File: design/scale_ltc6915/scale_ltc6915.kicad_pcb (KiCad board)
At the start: 2 copper layers, 70 x 40 mm, 76 parts, among them J1 USB_B_Micro, J2 Conn_02x03_Odd_Even, J3 Load cell, J4 Conn_01x04, Q1 IRLML6401, Q2 AO3400, Q3 AO3400, SW1 SW_SPST, SW2 ON/OFF switch, U1 MDBT42Q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

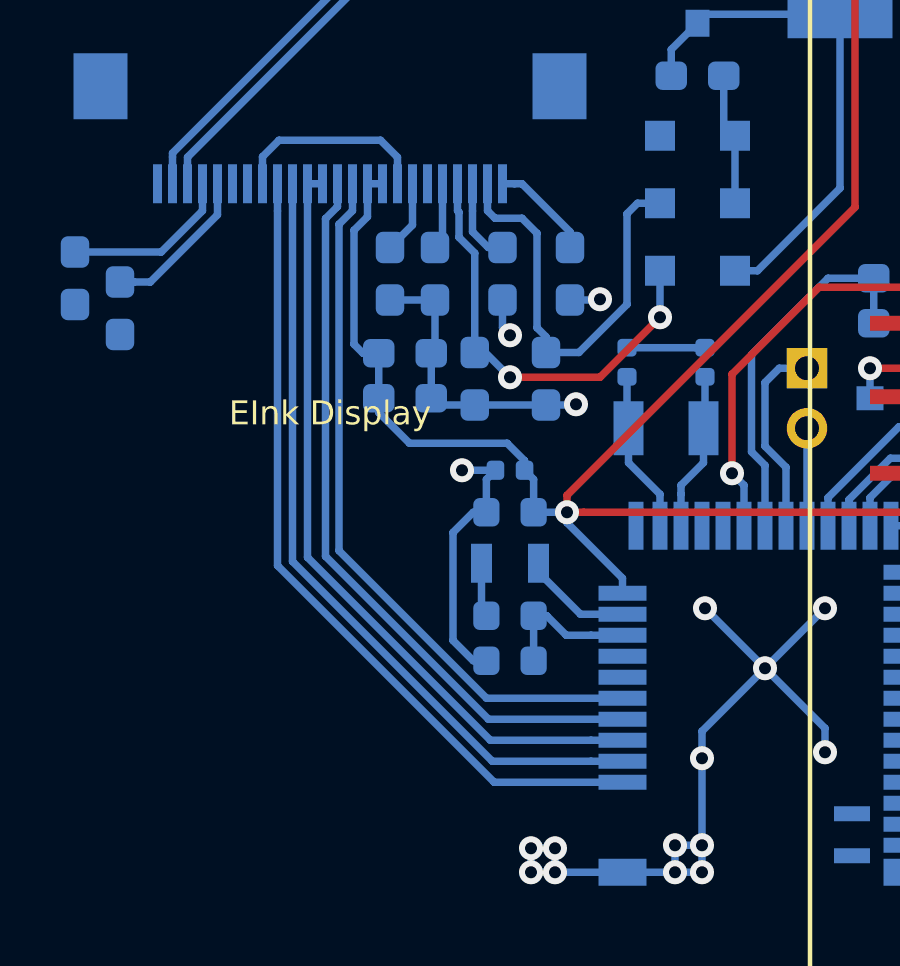
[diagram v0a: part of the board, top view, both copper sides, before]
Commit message: DC, CS pins separated, issue fixed. In both scale_hx711 and scale_ltc6915.
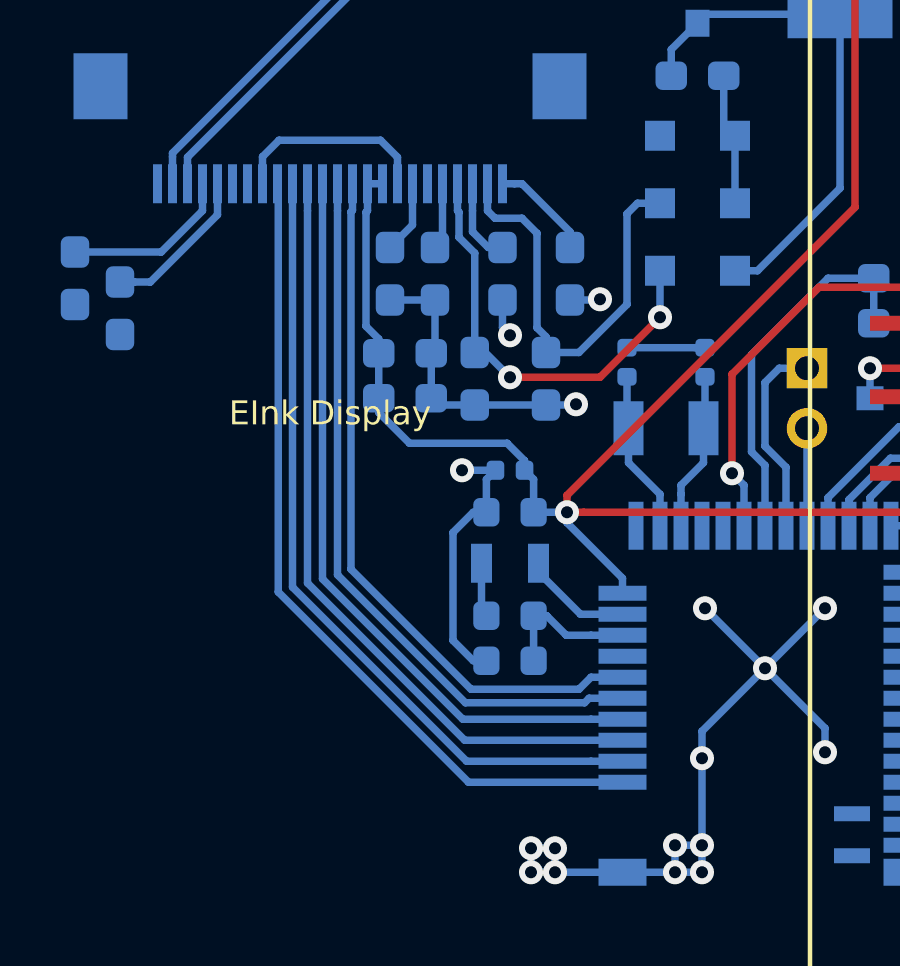
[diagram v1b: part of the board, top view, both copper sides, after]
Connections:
- EINK1 pad 11: /Sheet5E60241E/EINK_CS -> /Sheet5E60241E/EINK_DS
- U1 pad 4: /Sheet5E60241E/EINK_CS -> /Sheet5E60241E/EINK_DS
- U1 pad 5: /Sheet5E60241E/EINK_SCLK -> /Sheet5E60241E/EINK_CS
- U1 pad 6: /Sheet5E60241E/EINK_SDIO -> /Sheet5E60241E/EINK_SCLK
- U1 pad 7: (no net) -> /Sheet5E60241E/EINK_SDIO
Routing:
- net /Sheet5E60241E/EINK_DS: track 0.00 -> 26.0 mm
- net /Sheet5E60241E/EINK_CS: track 26.0 -> 25.1 mm
- net VDD: track 100.6 -> 100.0 mm
- net /Sheet5E60241E/EINK_RST: track 26.3 -> 26.8 mm
- net /Sheet5E60241E/EINK_BUSY: track 27.2 -> 27.7 mm
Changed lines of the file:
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@@
     (thickness 1.6)
     (drawings 17)
-    (tracks 583)
+    (tracks 589)
     (zones 0)
     (modules 76)
-    (nets 64)
+    (nets 65)
   )
   (page A4)
@@
   (net 62 /nRF/BT_LVL_EN)
   (net 63 /nRF/BAT_LVL)
+  (net 64 /Sheet5E60241E/EINK_DS)
   (net_class Default "This is the default net class."
     (clearance 0.2)
@@
     (add_net /Sheet5E60241E/EINK_BUSY)
     (add_net /Sheet5E60241E/EINK_CS)
+    (add_net /Sheet5E60241E/EINK_DS)
     (add_net /Sheet5E60241E/EINK_RST)
     (add_net /Sheet5E60241E/EINK_SCLK)
@@
       (net 40 /Sheet5E60241E/EINK_RST))
     (pad 11 smd rect (at -0.75 1.85) (size 0.3 1.3) (layers B.Cu B.Paste B.Mask)
-      (net 23 /Sheet5E60241E/EINK_CS))
+      (net 64 /Sheet5E60241E/EINK_DS))
     (pad 12 smd rect (at -0.25 1.85) (size 0.3 1.3) (layers B.Cu B.Paste B.Mask)
       (net 23 /Sheet5E60241E/EINK_CS))
@@
       (net 3 /nRF/DEC4))
     (pad 8 smd rect (at -4.75 -1.9) (size 1.6 0.5) (layers B.Cu B.Paste B.Mask))
-    (pad 7 smd rect (at -4.75 -1.2) (size 1.6 0.5) (layers B.Cu B.Paste B.Mask))
-    (pad 6 smd rect (at -4.75 -0.5) (size 1.6 0.5) (layers B.Cu B.Paste B.Mask)
+    (pad 7 smd rect (at -4.75 -1.2) (size 1.6 0.5) (layers B.Cu B.Paste B.Mask)
       (net 42 /Sheet5E60241E/EINK_SDIO))
-    (pad 5 smd rect (at -4.75 0.2) (size 1.6 0.5) (layers B.Cu B.Paste B.Mask)
+    (pad 6 smd rect (at -4.75 -0.5) (size 1.6 0.5) (layers B.Cu B.Paste B.Mask)
       (net 41 /Sheet5E60241E/EINK_SCLK))
-    (pad 4 smd rect (at -4.75 0.9) (size 1.6 0.5) (layers B.Cu B.Paste B.Mask)
+    (pad 5 smd rect (at -4.75 0.2) (size 1.6 0.5) (layers B.Cu B.Paste B.Mask)
       (net 23 /Sheet5E60241E/EINK_CS))
+    (pad 4 smd rect (at -4.75 0.9) (size 1.6 0.5) (layers B.Cu B.Paste B.Mask)
+      (net 64 /Sheet5E60241E/EINK_DS))
     (pad 3 smd rect (at -4.75 1.6) (size 1.6 0.5) (layers B.Cu B.Paste B.Mask)
       (net 40 /Sheet5E60241E/EINK_RST))
@@
   (segment (start 48.5 13.5) (end 49 13) (width 0.25) (layer B.Cu) (net 5))
   (segment (start 33.25 22.85) (end 32.75 22.85) (width 0.25) (layer B.Cu) (net 5))
-  (segment (start 32.75 22.85) (end 32.75 23.95) (width 0.25) (layer B.Cu) (net 5))
-  (segment (start 32.75 23.95) (end 32.3 24.4) (width 0.25) (layer B.Cu) (net 5))
-  (segment (start 32.6 28.5) (end 33.125 28.5) (width 0.25) (layer B.Cu) (net 5))
-  (segment (start 32.3 28.2) (end 32.6 28.5) (width 0.25) (layer B.Cu) (net 5))
-  (segment (start 32.3 24.4) (end 32.3 28.2) (width 0.25) (layer B.Cu) (net 5))
   (via (at 39.4 33.8) (size 0.8) (drill 0.4) (layers F.Cu B.Cu) (net 5))
   (segment (start 39.4 34.15) (end 39.4 33.8) (width 0.25) (layer B.Cu) (net 5))
@@
   (segment (start 66.2 11.6) (end 65.7 12.1) (width 0.25) (layer B.Cu) (net 5))
   (segment (start 67.6 11.6) (end 66.2 11.6) (width 0.25) (layer B.Cu) (net 5))
+  (segment (start 33.125 28.025) (end 33.125 28.5) (width 0.25) (layer B.Cu) (net 5))
+  (segment (start 32.69999 27.59999) (end 33.125 28.025) (width 0.25) (layer B.Cu) (net 5))
+  (segment (start 32.69999 23.80001) (end 32.69999 27.59999) (width 0.25) (layer B.Cu) (net 5))
+  (segment (start 32.75 23.75) (end 32.69999 23.80001) (width 0.25) (layer B.Cu) (net 5))
+  (segment (start 32.75 22.85) (end 32.75 23.75) (width 0.25) (layer B.Cu) (net 5))
   (segment (start 41.4 30.95) (end 41.45 31) (width 0.25) (layer B.Cu) (net 6))
   (segment (start 41.4 29.285) (end 41.4 30.95) (width 0.25) (layer B.Cu) (net 6))
@@
   (segment (start 44.4 16.5) (end 44.7 16.2) (width 0.25) (layer B.Cu) (net 22))
   (segment (start 32.214998 16.5) (end 44.4 16.5) (width 0.25) (layer B.Cu) (net 22))
-  (segment (start 31.25 22.85) (end 30.75 22.85) (width 0.25) (layer B.Cu) (net 23))
-  (segment (start 40.2 41.4) (end 41.25 41.4) (width 0.25) (layer B.Cu) (net 23))
-  (segment (start 30.75 35.304314) (end 36.845686 41.4) (width 0.25) (layer B.Cu) (net 23))
-  (segment (start 36.845686 41.4) (end 40.2 41.4) (width 0.25) (layer B.Cu) (net 23))
-  (segment (start 30.75 22.85) (end 30.75 35.304314) (width 0.25) (layer B.Cu) (net 23))
+  (segment (start 40.2 40.7) (end 41.25 40.7) (width 0.25) (layer B.Cu) (net 23))
+  (segment (start 35.927182 40.7) (end 40.2 40.7) (width 0.25) (layer B.Cu) (net 23))
+  (segment (start 31.25 36.022818) (end 35.927182 40.7) (width 0.25) (layer B.Cu) (net 23))
+  (segment (start 31.25 22.85) (end 31.25 36.022818) (width 0.25) (layer B.Cu) (net 23))
   (segment (start 51.8 44.2) (end 50.75 44.2) (width 0.25) (layer B.Cu) (net 25))
   (segment (start 52.775 44.2) (end 51.8 44.2) (width 0.25) (layer B.Cu) (net 25))
@@
   (segment (start 57.15 26.3) (end 57.875 27.025) (width 0.25) (layer B.Cu) (net 38))
   (segment (start 53.6 26.3) (end 57.15 26.3) (width 0.25) (layer B.Cu) (net 38))
-  (segment (start 29.75 35.577134) (end 29.75 23.75) (width 0.25) (layer B.Cu) (net 39))
-  (segment (start 29.75 23.75) (end 29.75 22.85) (width 0.25) (layer B.Cu) (net 39))
-  (segment (start 36.972866 42.8) (end 29.75 35.577134) (width 0.25) (layer B.Cu) (net 39))
-  (segment (start 41.25 42.8) (end 36.972866 42.8) (width 0.25) (layer B.Cu) (net 39))
+  (segment (start 29.774999 22.874999) (end 29.75 22.85) (width 0.25) (layer B.Cu) (net 39))
+  (segment (start 29.774999 36.457047) (end 29.774999 22.874999) (width 0.25) (layer B.Cu) (net 39))
+  (segment (start 41.25 42.8) (end 36.117952 42.8) (width 0.25) (layer B.Cu) (net 39))
+  (segment (start 36.117952 42.8) (end 29.774999 36.457047) (width 0.25) (layer B.Cu) (net 39))
   (segment (start 40.2 42.1) (end 41.25 42.1) (width 0.25) (layer B.Cu) (net 40))
-  (segment (start 30.25 35.440724) (end 36.909276 42.1) (width 0.25) (layer B.Cu) (net 40))
-  (segment (start 36.909276 42.1) (end 40.2 42.1) (width 0.25) (layer B.Cu) (net 40))
-  (segment (start 30.25 22.85) (end 30.25 35.440724) (width 0.25) (layer B.Cu) (net 40))
-  (segment (start 31.75 23.61359) (end 31.75 22.85) (width 0.25) (layer B.Cu) (net 41))
-  (segment (start 31.349991 24.013599) (end 31.75 23.61359) (width 0.25) (layer B.Cu) (net 41))
-  (segment (start 36.782096 40.7) (end 31.34999 35.267894) (width 0.25) (layer B.Cu) (net 41))
-  (segment (start 31.34999 35.267894) (end 31.349991 24.013599) (width 0.25) (layer B.Cu) (net 41))
-  (segment (start 41.25 40.7) (end 36.782096 40.7) (width 0.25) (layer B.Cu) (net 41))
-  (segment (start 32.25 23.75) (end 32.25 22.85) (width 0.25) (layer B.Cu) (net 42))
-  (segment (start 31.8 24.2) (end 32.25 23.75) (width 0.25) (layer B.Cu) (net 42))
-  (segment (start 36.718506 40) (end 31.8 35.081494) (width 0.25) (layer B.Cu) (net 42))
-  (segment (start 31.8 35.081494) (end 31.8 24.2) (width 0.25) (layer B.Cu) (net 42))
-  (segment (start 41.25 40) (end 36.718506 40) (width 0.25) (layer B.Cu) (net 42))
+  (segment (start 36.054362 42.1) (end 40.2 42.1) (width 0.25) (layer B.Cu) (net 40))
+  (segment (start 30.25 36.295638) (end 36.054362 42.1) (width 0.25) (layer B.Cu) (net 40))
+  (segment (start 30.25 22.85) (end 30.25 36.295638) (width 0.25) (layer B.Cu) (net 40))
+  (segment (start 36.013599 40.150009) (end 31.75 35.88641) (width 0.25) (layer B.Cu) (net 41))
+  (segment (start 39.9864 40.15001) (end 36.013599 40.150009) (width 0.25) (layer B.Cu) (net 41))
+  (segment (start 31.75 23.75) (end 31.75 22.85) (width 0.25) (layer B.Cu) (net 41))
+  (segment (start 40.13641 40) (end 39.9864 40.15001) (width 0.25) (layer B.Cu) (net 41))
+  (segment (start 31.75 35.88641) (end 31.75 23.75) (width 0.25) (layer B.Cu) (net 41))
+  (segment (start 41.25 40) (end 40.13641 40) (width 0.25) (layer B.Cu) (net 41))
+  (segment (start 32.25 23.735002) (end 32.2 23.785002) (width 0.25) (layer B.Cu) (net 42))
+  (segment (start 32.25 22.85) (end 32.25 23.735002) (width 0.25) (layer B.Cu) (net 42))
+  (segment (start 32.2 23.785002) (end 32.2 35.7) (width 0.25) (layer B.Cu) (net 42))
+  (segment (start 32.2 35.7) (end 36.2 39.7) (width 0.25) (layer B.Cu) (net 42))
+  (segment (start 40.2 39.3) (end 41.25 39.3) (width 0.25) (layer B.Cu) (net 42))
+  (segment (start 39.8 39.7) (end 40.2 39.3) (width 0.25) (layer B.Cu) (net 42))
+  (segment (start 36.2 39.7) (end 39.8 39.7) (width 0.25) (layer B.Cu) (net 42))
   (via (at 60 32) (size 0.8) (drill 0.4) (layers F.Cu B.Cu) (net 43))
   (via (at 60.6 21.5) (size 0.8) (drill 0.4) (layers F.Cu B.Cu) (net 43))
@@
   (segment (start 48.1 26) (end 49.625 26) (width 0.25) (layer B.Cu) (net 63))
   (segment (start 45.549991 28.550009) (end 48.1 26) (width 0.25) (layer B.Cu) (net 63))
+  (segment (start 30.75 23.75) (end 30.75 22.85) (width 0.25) (layer B.Cu) (net 64))
+  (segment (start 30.75 36.159228) (end 30.75 23.75) (width 0.25) (layer B.Cu) (net 64))
+  (segment (start 35.990772 41.4) (end 30.75 36.159228) (width 0.25) (layer B.Cu) (net 64))
+  (segment (start 41.25 41.4) (end 35.990772 41.4) (width 0.25) (layer B.Cu) (net 64))
   (zone (net 0) (net_name "") (layers F&B.Cu) (hatch edge 0.508)
     (connect_pads (clearance 0.508))
